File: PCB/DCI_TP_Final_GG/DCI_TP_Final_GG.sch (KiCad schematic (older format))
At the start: 0 parts

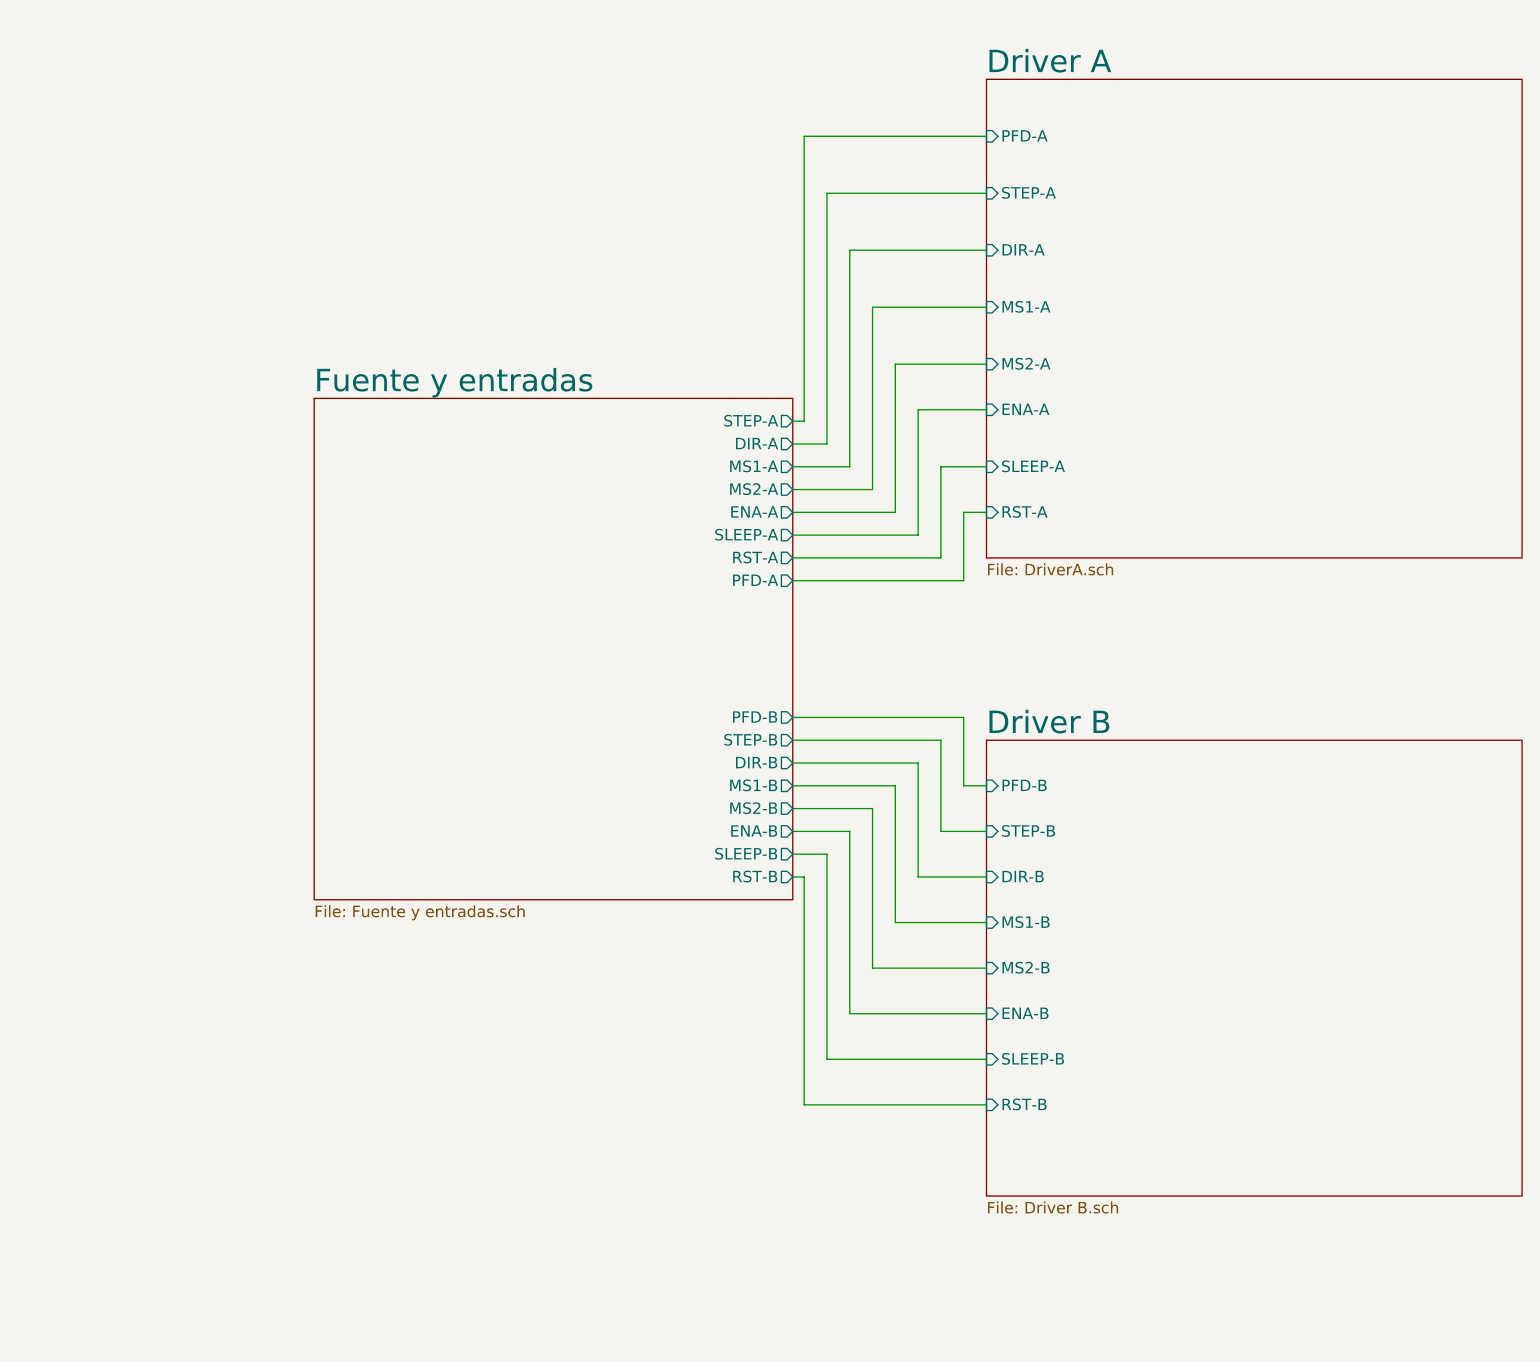
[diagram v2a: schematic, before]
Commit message: Se completo el esquematico y documentación. El esquematico esta listo para una primera revisión.
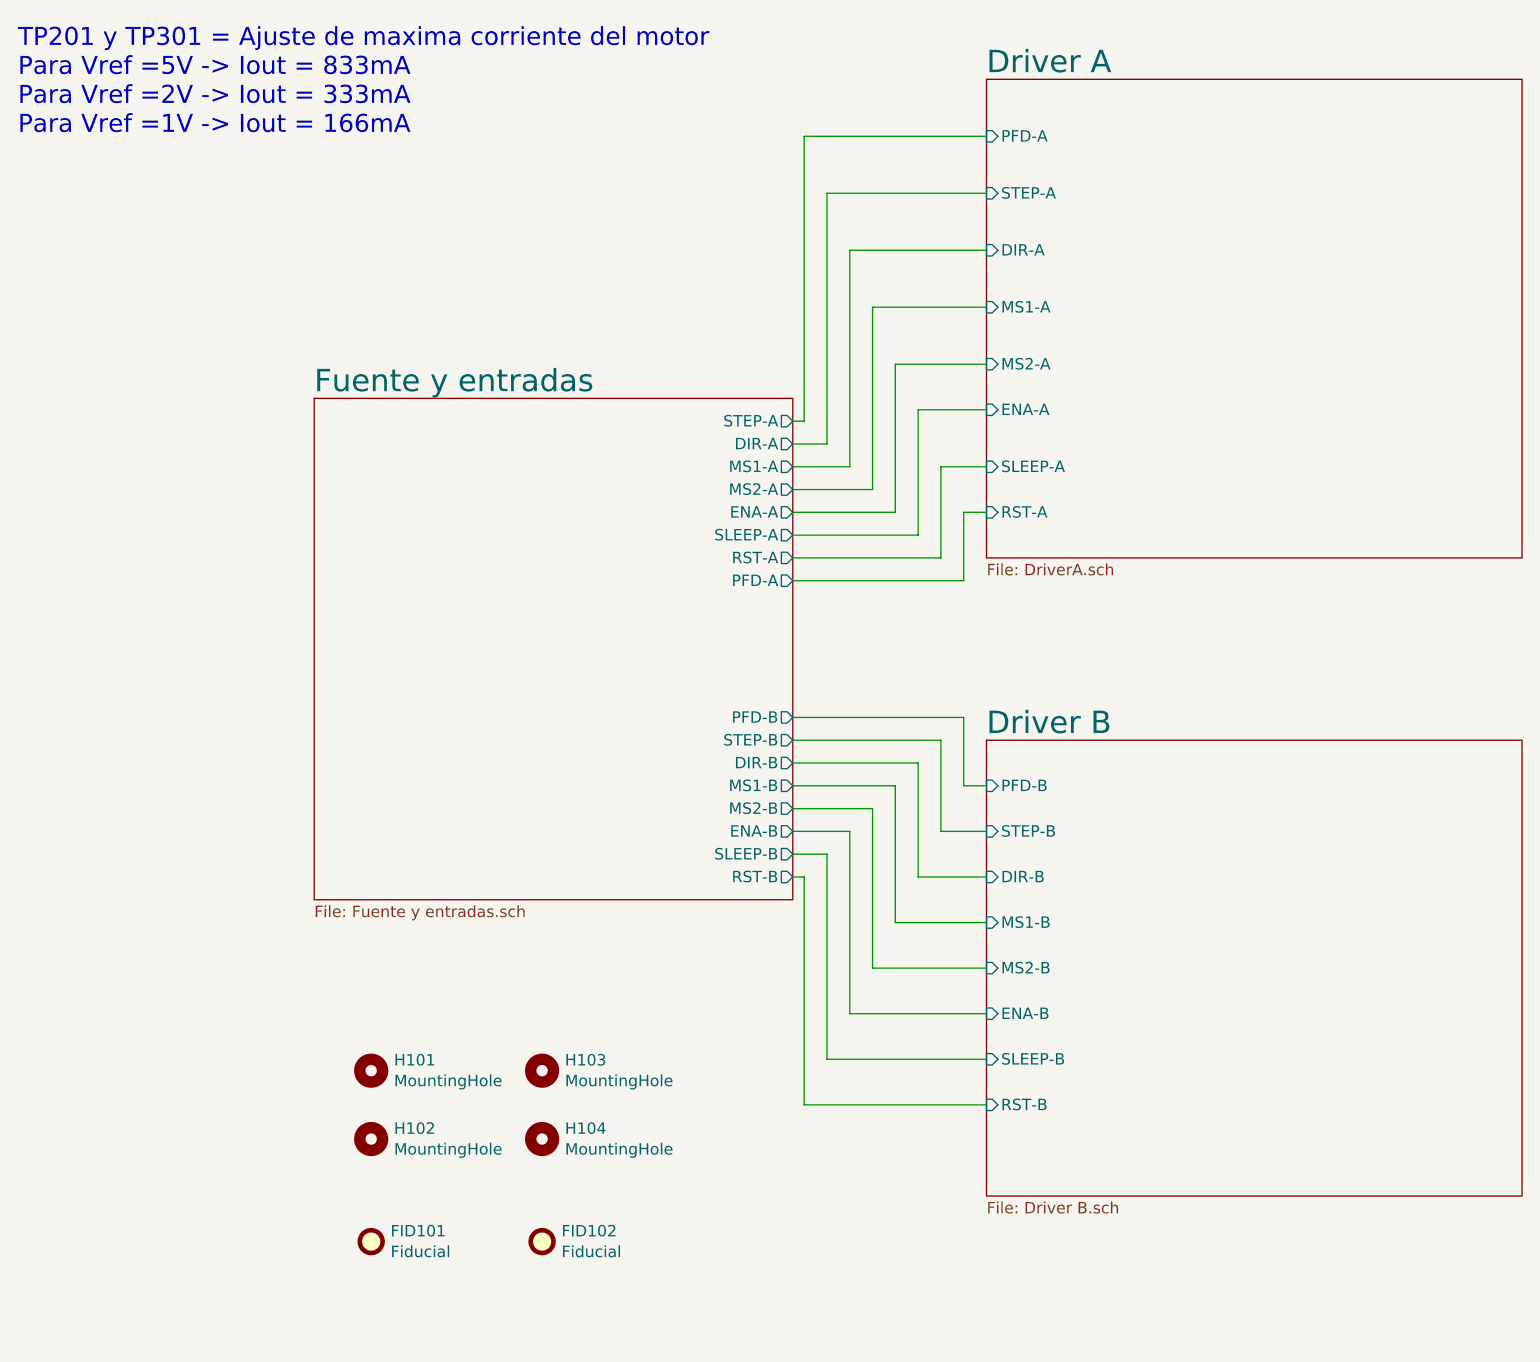
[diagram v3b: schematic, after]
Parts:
- added FID101, FID102: Fiducial, Fiducial:Fiducial_1mm_Mask2mm, symbol Mechanical:Fiducial
- added H101, H102, H103, H104: MountingHole, MountingHole:MountingHole_3mm, symbol Mechanical:MountingHole
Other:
- note added: "TP201 y TP301 = Ajuste de maxima corriente del motor\nPara Vref =5V -> Iout = 833mA\nPara Vref =2V -> Iout = 333mA\nPara Vref =1V -> Iout = 166mA"
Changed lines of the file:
@@
 F17 "PFD-B" O R 4800 3900 50
 $EndSheet
+$Comp
+L Mechanical:MountingHole H101
+U 1 1 5D99080F
+P 2950 5450
+F 0 "H101" H 3050 5496 50  0000 L CNN
+F 1 "MountingHole" H 3050 5405 50  0000 L CNN
+F 2 "MountingHole:MountingHole_3mm" H 2950 5450 50  0001 C CNN
+F 3 "" H 2950 5450 50  0001 C CNN
+	1    2950 5450
+	1    0    0    -1
+$EndComp
+$Comp
+L Mechanical:MountingHole H103
+U 1 1 5D990B77
+P 3700 5450
+F 0 "H103" H 3800 5496 50  0000 L CNN
+F 1 "MountingHole" H 3800 5405 50  0000 L CNN
+F 2 "MountingHole:MountingHole_3mm" H 3700 5450 50  0001 C CNN
+F 3 "" H 3700 5450 50  0001 C CNN
+	1    3700 5450
+	1    0    0    -1
+$EndComp
+$Comp
+L Mechanical:MountingHole H102
+U 1 1 5D990F21
+P 2950 5750
+F 0 "H102" H 3050 5796 50  0000 L CNN
+F 1 "MountingHole" H 3050 5705 50  0000 L CNN
+F 2 "MountingHole:MountingHole_3mm" H 2950 5750 50  0001 C CNN
+F 3 "" H 2950 5750 50  0001 C CNN
+	1    2950 5750
+	1    0    0    -1
+$EndComp
+$Comp
+L Mechanical:MountingHole H104
+U 1 1 5D990FED
+P 3700 5750
+F 0 "H104" H 3800 5796 50  0000 L CNN
+F 1 "MountingHole" H 3800 5705 50  0000 L CNN
+F 2 "MountingHole:MountingHole_3mm" H 3700 5750 50  0001 C CNN
+F 3 "" H 3700 5750 50  0001 C CNN
+	1    3700 5750
+	1    0    0    -1
+$EndComp
+$Comp
+L Mechanical:Fiducial FID101
+U 1 1 5D991143
+P 2950 6200
+F 0 "FID101" H 3035 6246 50  0000 L CNN
+F 1 "Fiducial" H 3035 6155 50  0000 L CNN
+F 2 "Fiducial:Fiducial_1mm_Mask2mm" H 2950 6200 50  0001 C CNN
+F 3 "~" H 2950 6200 50  0001 C CNN
+	1    2950 6200
+	1    0    0    -1
+$EndComp
+$Comp
+L Mechanical:Fiducial FID102
+U 1 1 5D991272
+P 3700 6200
+F 0 "FID102" H 3785 6246 50  0000 L CNN
+F 1 "Fiducial" H 3785 6155 50  0000 L CNN
+F 2 "Fiducial:Fiducial_1mm_Mask2mm" H 3700 6200 50  0001 C CNN
+F 3 "~" H 3700 6200 50  0001 C CNN
+	1    3700 6200
+	1    0    0    -1
+$EndComp
+Text Notes 1400 1350 0    79   ~ 0
+TP201 y TP301 = Ajuste de maxima corriente del motor\nPara Vref =5V -> Iout = 833mA\nPara Vref =2V -> Iout = 333mA\nPara Vref =1V -> Iout = 166mA
 $EndSCHEMATC

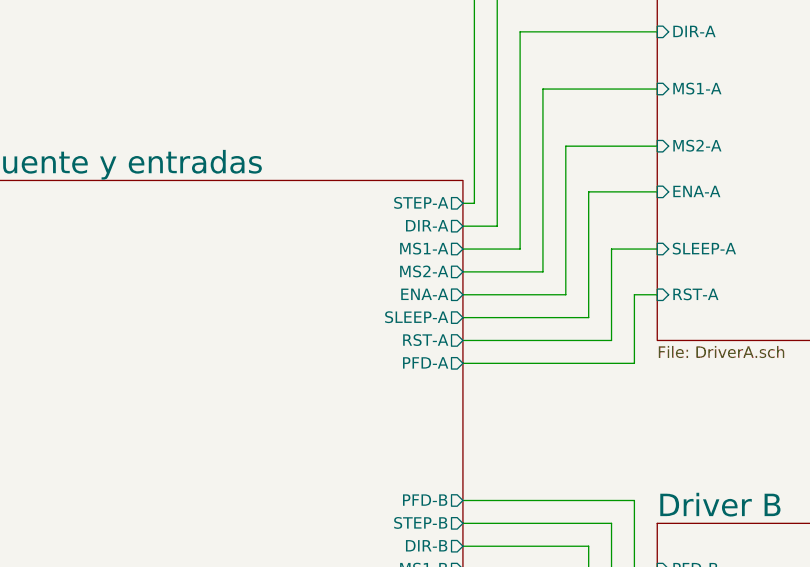
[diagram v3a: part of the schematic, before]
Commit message: Inicio etapa de desarrollo de PCB, agrego biblioteca de borneras
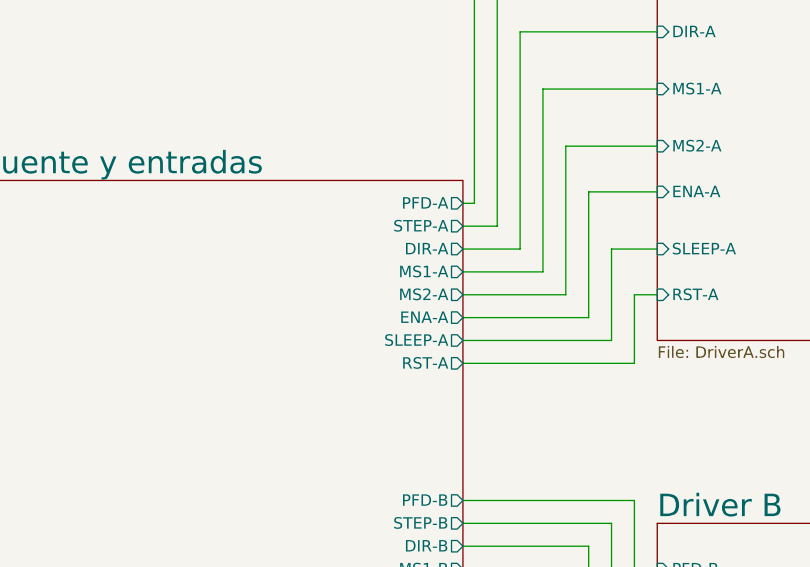
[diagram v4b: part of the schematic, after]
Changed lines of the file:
@@
 	4800 3300 5550 3300
-Wire Wire Line
-	5550 3300 5550 3000
-Wire Wire Line
-	5550 3000 5650 3000
 Wire Wire Line
 	4800 3200 5450 3200
 Wire Wire Line
 	5450 3200 5450 2800
-Wire Wire Line
-	5450 2800 5650 2800
 Wire Wire Line
 	4800 3100 5350 3100
@@
 Wire Wire Line
 	4850 1350 5650 1350
-$Sheet
-S 2700 2500 2100 2200
-U 5D973A64
-F0 "Fuente y entradas" 98
-F1 "Fuente y entradas.sch" 50
-F2 "MS1-A" O R 4800 2800 50
-F3 "MS2-A" O R 4800 2900 50
-F4 "ENA-A" O R 4800 3000 50
-F5 "SLEEP-A" O R 4800 3100 50
-F6 "RST-A" O R 4800 3200 50
-F7 "STEP-A" O R 4800 2600 50
-F8 "DIR-A" O R 4800 2700 50
-F9 "PFD-A" O R 4800 3300 50
-F10 "MS1-B" O R 4800 4200 50
-F11 "MS2-B" O R 4800 4300 50
-F12 "ENA-B" O R 4800 4400 50
-F13 "SLEEP-B" O R 4800 4500 50
-F14 "RST-B" O R 4800 4600 50
-F15 "STEP-B" O R 4800 4000 50
-F16 "DIR-B" O R 4800 4100 50
-F17 "PFD-B" O R 4800 3900 50
-$EndSheet
 $Comp
 L Mechanical:MountingHole H101
@@
 Text Notes 1400 1350 0    79   ~ 0
 TP201 y TP301 = Ajuste de maxima corriente del motor\nPara Vref =5V -> Iout = 833mA\nPara Vref =2V -> Iout = 333mA\nPara Vref =1V -> Iout = 166mA
+$Sheet
+S 2700 2500 2100 2200
+U 5D973A64
+F0 "Fuente y entradas" 98
+F1 "Fuente y entradas.sch" 50
+F2 "MS1-A" O R 4800 2900 50
+F3 "MS2-A" O R 4800 3000 50
+F4 "ENA-A" O R 4800 3100 50
+F5 "SLEEP-A" O R 4800 3200 50
+F6 "RST-A" O R 4800 3300 50
+F7 "STEP-A" O R 4800 2700 50
+F8 "DIR-A" O R 4800 2800 50
+F9 "PFD-A" O R 4800 2600 50
+F10 "MS1-B" O R 4800 4200 50
+F11 "MS2-B" O R 4800 4300 50
+F12 "ENA-B" O R 4800 4400 50
+F13 "SLEEP-B" O R 4800 4500 50
+F14 "RST-B" O R 4800 4600 50
+F15 "STEP-B" O R 4800 4000 50
+F16 "DIR-B" O R 4800 4100 50
+F17 "PFD-B" O R 4800 3900 50
+$EndSheet
+Wire Wire Line
+	5450 2800 5650 2800
+Wire Wire Line
+	5550 3000 5650 3000
+Wire Wire Line
+	5550 3300 5550 3000
 $EndSCHEMATC

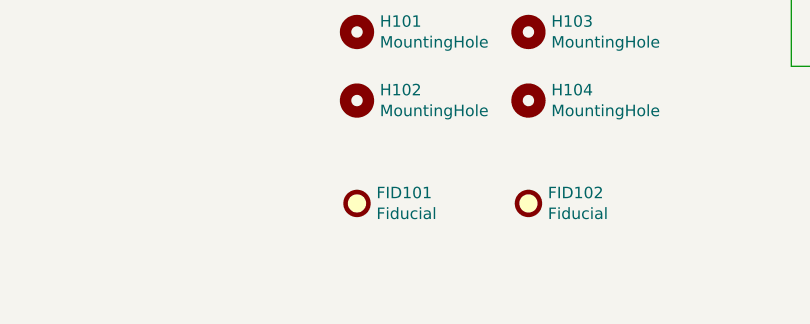
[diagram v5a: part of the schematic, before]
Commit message: Cambio de ubicacion de capacitores de desacople en la jerarquia del esquematico y actualizacion de identificadores en PCB
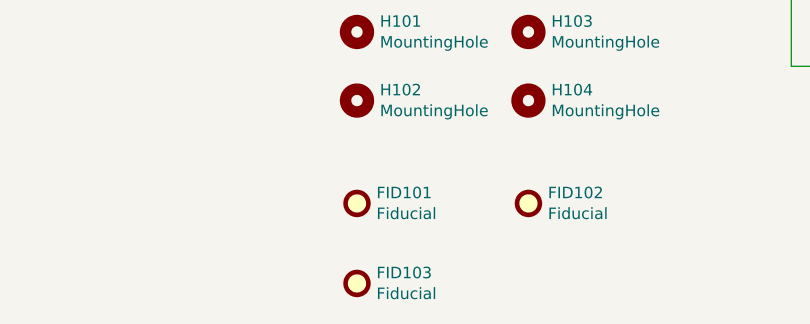
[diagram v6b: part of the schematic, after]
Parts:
- added FID103: Fiducial, Fiducial:Fiducial_1mm_Mask2mm, symbol Mechanical:Fiducial
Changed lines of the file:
@@
 Sheet 1 4
 Title "Replica Dual EasyDriver v4.5"
-Date "2019-10-02"
-Rev "Matias Brignone"
+Date "2019-10-26"
+Rev "M Brignone"
 Comp "Gonzalo Gontad - CESE-FIUBA"
-Comment1 ""
+Comment1 "Revisores: M. Ribelotta y M. Brignone"
 Comment2 ""
 Comment3 ""
@@
 Wire Wire Line
 	5550 3300 5550 3000
+$Comp
+L Mechanical:Fiducial FID103
+U 1 1 5DAEF19A
+P 2950 6550
+F 0 "FID103" H 3035 6596 50  0000 L CNN
+F 1 "Fiducial" H 3035 6505 50  0000 L CNN
+F 2 "Fiducial:Fiducial_1mm_Mask2mm" H 2950 6550 50  0001 C CNN
+F 3 "~" H 2950 6550 50  0001 C CNN
+	1    2950 6550
+	1    0    0    -1
+$EndComp
 $EndSCHEMATC
